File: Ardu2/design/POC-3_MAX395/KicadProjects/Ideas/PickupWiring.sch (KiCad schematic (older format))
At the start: 2 parts

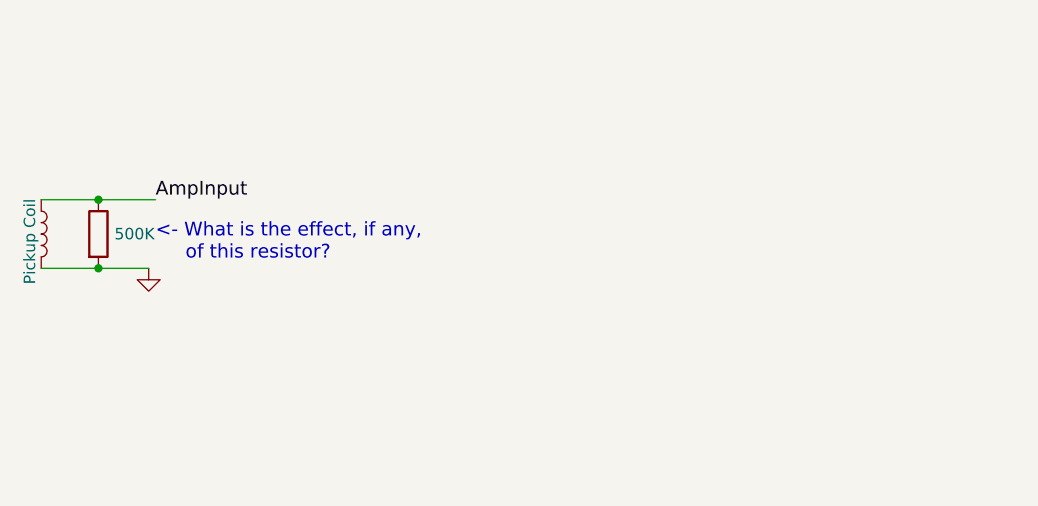
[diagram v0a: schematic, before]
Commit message: added schematics for std and reverse pot volume wiring
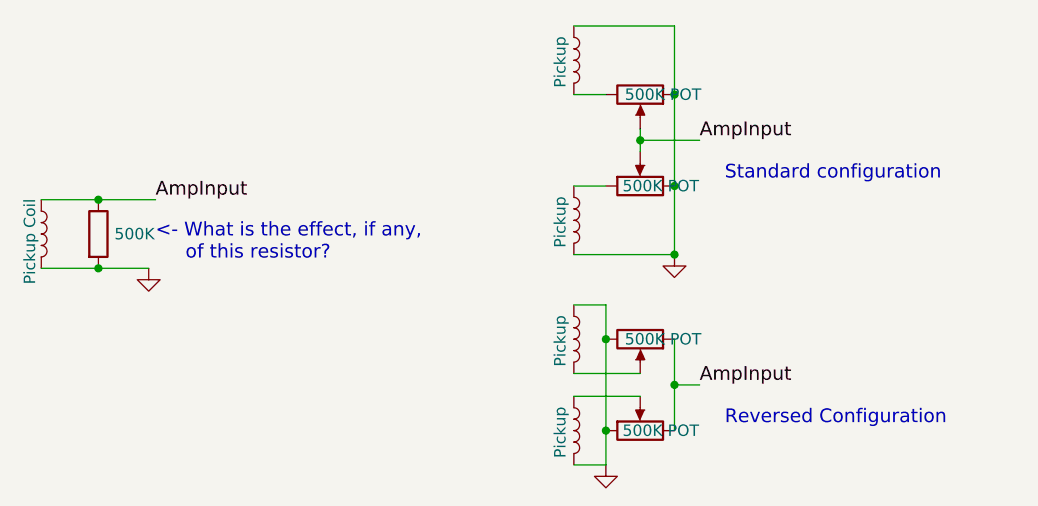
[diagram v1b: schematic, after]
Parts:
- added L? (x4): Pickup, symbol L
- added RV? (x4): 500K POT, symbol POT
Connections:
- wire segments 2 -> 24
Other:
- note added: "Reversed Configuration"
- note added: "Standard configuration"
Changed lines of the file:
@@
 LIBS:contrib
 LIBS:valves
+LIBS:PickupWiring-cache
 EELAYER 26 0
 EELAYER END
@@
 $EndComp
 $Comp
-L GND #PWR?
+L GND #PWR01
 U 1 1 586A50A6
 P 3260 3280
-F 0 "#PWR?" H 3260 3030 50  0001 C CNN
+F 0 "#PWR01" H 3260 3030 50  0001 C CNN
 F 1 "GND" H 3265 3109 50  0001 C CNN
 F 2 "" H 3260 3280 50  0000 C CNN
@@
 $EndComp
 Wire Wire Line
-	2790 3280 3260 3280
+	2790 3280 3040 3280
+Wire Wire Line
+	3040 3280 3260 3280
 Connection ~ 3040 3280
 Wire Wire Line
-	2790 2980 3290 2980
+	2790 2980 3040 2980
+Wire Wire Line
+	3040 2980 3290 2980
 Connection ~ 3040 2980
 Text Label 3290 2980 0    60   ~ 0
@@
 Text Notes 3290 3250 0    60   ~ 0
 <- What is the effect, if any,\n     of this resistor?
+$Comp
+L POT RV?
+U 1 1 586CC04C
+P 5410 2520
+F 0 "RV?" V 5206 2520 50  0001 C CNN
+F 1 "500K POT" V 5410 2620 50  0000 C CNN
+F 2 "" H 5410 2520 50  0000 C CNN
+F 3 "" H 5410 2520 50  0000 C CNN
+	1    5410 2520
+	0    1    1    0
+$EndComp
+$Comp
+L POT RV?
+U 1 1 586CC096
+P 5410 2920
+F 0 "RV?" V 5296 2920 50  0001 C CNN
+F 1 "500K POT" V 5410 2830 50  0000 C CNN
+F 2 "" H 5410 2920 50  0000 C CNN
+F 3 "" H 5410 2920 50  0000 C CNN
+	1    5410 2920
+	0    -1   -1   0
+$EndComp
+$Comp
+L L L?
+U 1 1 586CC199
+P 5120 2370
+F 0 "L?" H 5172 2415 50  0001 L CNN
+F 1 "Pickup" V 5060 2250 50  0000 L CNN
+F 2 "" H 5120 2370 50  0000 C CNN
+F 3 "" H 5120 2370 50  0000 C CNN
+	1    5120 2370
+	1    0    0    -1
+$EndComp
+$Comp
+L GND #PWR02
+U 1 1 586CC3DF
+P 5560 3220
+F 0 "#PWR02" H 5560 2970 50  0001 C CNN
+F 1 "GND" H 5565 3049 50  0001 C CNN
+F 2 "" H 5560 3220 50  0000 C CNN
+F 3 "" H 5560 3220 50  0000 C CNN
+	1    5560 3220
+	1    0    0    -1
+$EndComp
+Wire Wire Line
+	5120 2520 5260 2520
+Wire Wire Line
+	5120 2920 5260 2920
+Wire Wire Line
+	5560 3220 5120 3220
+Wire Wire Line
+	5560 2220 5560 2520
+Wire Wire Line
+	5560 2520 5560 2920
+Wire Wire Line
+	5560 2920 5560 3220
+Connection ~ 5560 3220
+Connection ~ 5560 2920
+Wire Wire Line
+	5120 2220 5560 2220
+Connection ~ 5560 2520
+Wire Wire Line
+	5410 2670 5410 2720
+Wire Wire Line
+	5410 2720 5410 2770
+Connection ~ 5410 2720
+Wire Wire Line
+	5410 2720 5670 2720
+Text Label 5670 2720 0    60   ~ 0
+AmpInput
+$Comp
+L L L?
+U 1 1 586CC632
+P 5120 3070
+F 0 "L?" H 5172 3115 50  0001 L CNN
+F 1 "Pickup" V 5060 2950 50  0000 L CNN
+F 2 "" H 5120 3070 50  0000 C CNN
+F 3 "" H 5120 3070 50  0000 C CNN
+	1    5120 3070
+	1    0    0    -1
+$EndComp
+$Comp
+L POT RV?
+U 1 1 586CC63D
+P 5410 3590
+F 0 "RV?" V 5206 3590 50  0001 C CNN
+F 1 "500K POT" V 5410 3690 50  0000 C CNN
+F 2 "" H 5410 3590 50  0000 C CNN
+F 3 "" H 5410 3590 50  0000 C CNN
+	1    5410 3590
+	0    1    1    0
+$EndComp
+$Comp
+L POT RV?
+U 1 1 586CC643
+P 5410 3990
+F 0 "RV?" V 5296 3990 50  0001 C CNN
+F 1 "500K POT" V 5410 3900 50  0000 C CNN
+F 2 "" H 5410 3990 50  0000 C CNN
+F 3 "" H 5410 3990 50  0000 C CNN
+	1    5410 3990
+	0    -1   -1   0
+$EndComp
+$Comp
+L L L?
+U 1 1 586CC649
+P 5120 3590
+F 0 "L?" H 5172 3635 50  0001 L CNN
+F 1 "Pickup" V 5060 3470 50  0000 L CNN
+F 2 "" H 5120 3590 50  0000 C CNN
+F 3 "" H 5120 3590 50  0000 C CNN
+	1    5120 3590
+	1    0    0    -1
+$EndComp
+$Comp
+L GND #PWR03
+U 1 1 586CC64F
+P 5260 4140
+F 0 "#PWR03" H 5260 3890 50  0001 C CNN
+F 1 "GND" H 5265 3969 50  0001 C CNN
+F 2 "" H 5260 4140 50  0000 C CNN
+F 3 "" H 5260 4140 50  0000 C CNN
+	1    5260 4140
+	1    0    0    -1
+$EndComp
+Text Label 5670 3790 0    60   ~ 0
+AmpInput
+$Comp
+L L L?
+U 1 1 586CC661
+P 5120 3990
+F 0 "L?" H 5172 4035 50  0001 L CNN
+F 1 "Pickup" V 5060 3870 50  0000 L CNN
+F 2 "" H 5120 3990 50  0000 C CNN
+F 3 "" H 5120 3990 50  0000 C CNN
+	1    5120 3990
+	1    0    0    -1
+$EndComp
+Wire Wire Line
+	5560 3590 5560 3790
+Wire Wire Line
+	5560 3790 5560 3990
+Wire Wire Line
+	5560 3790 5670 3790
+Connection ~ 5560 3790
+Wire Wire Line
+	5120 3840 5410 3840
+Wire Wire Line
+	5120 3740 5410 3740
+Wire Wire Line
+	5120 3440 5260 3440
+Connection ~ 5260 3990
+Connection ~ 5260 3590
+Wire Wire Line
+	5260 3440 5260 3590
+Wire Wire Line
+	5260 3590 5260 3990
+Wire Wire Line
+	5260 4140 5260 4000
+Wire Wire Line
+	5120 4140 5260 4140
+Text Notes 5780 2900 0    60   ~ 0
+Standard configuration
+Text Notes 5780 3970 0    60   ~ 0
+Reversed Configuration
 $EndSCHEMATC
